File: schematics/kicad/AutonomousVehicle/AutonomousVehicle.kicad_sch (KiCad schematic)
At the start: 18 parts, among them J1 Raspberry Pi 4, J2 SENSOR_FL, J3 SENSOR_RL, J4 SENSOR_FR, J5 SENSOR_RR, J6 MOTOR_LEFT, J7 MOTOR_RIGHT, U1 L298N

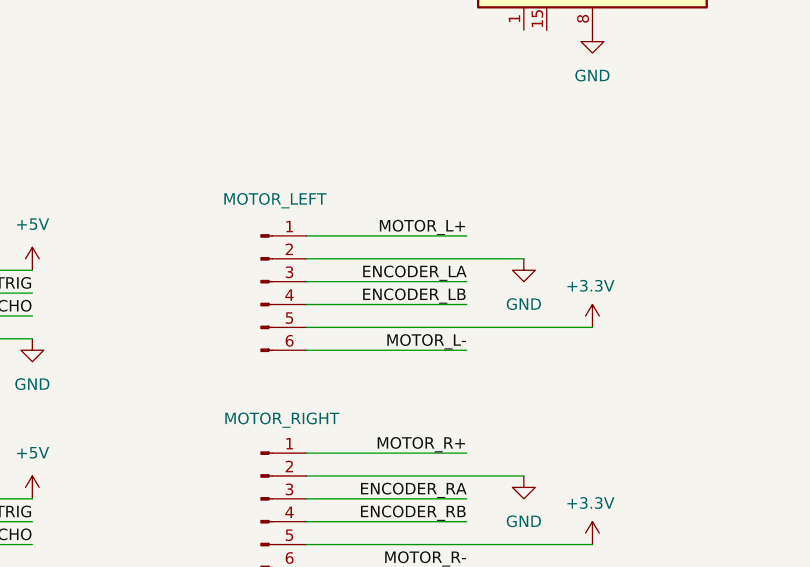
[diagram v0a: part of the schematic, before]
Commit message: add logger
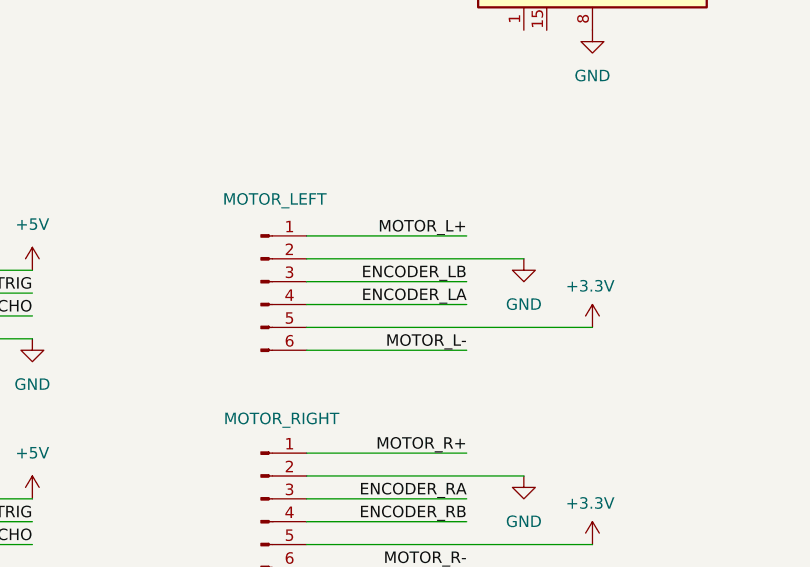
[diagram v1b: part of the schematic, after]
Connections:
- net ENCODER_LA: now also J6.4 (Pin_4); no longer J6.3 (Pin_3)
- net ENCODER_LB: now also J6.3 (Pin_3); no longer J6.4 (Pin_4)
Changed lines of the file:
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@@
 		)
 	)
-	(label "ENCODER_LA"
+	(label "ENCODER_LB"
 		(at 134.62 151.13 180)
 		(fields_autoplaced yes)
@@
 		)
 	)
-	(label "ENCODER_LB"
+	(label "ENCODER_LA"
 		(at 134.62 153.67 180)
 		(fields_autoplaced yes)
